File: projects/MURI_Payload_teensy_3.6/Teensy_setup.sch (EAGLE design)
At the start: 54 parts, among them IC1 DS18B20, IC2 DS18B20, IC4 DS18B20, IC5 DS18B20, U2 MS560702BA03-50

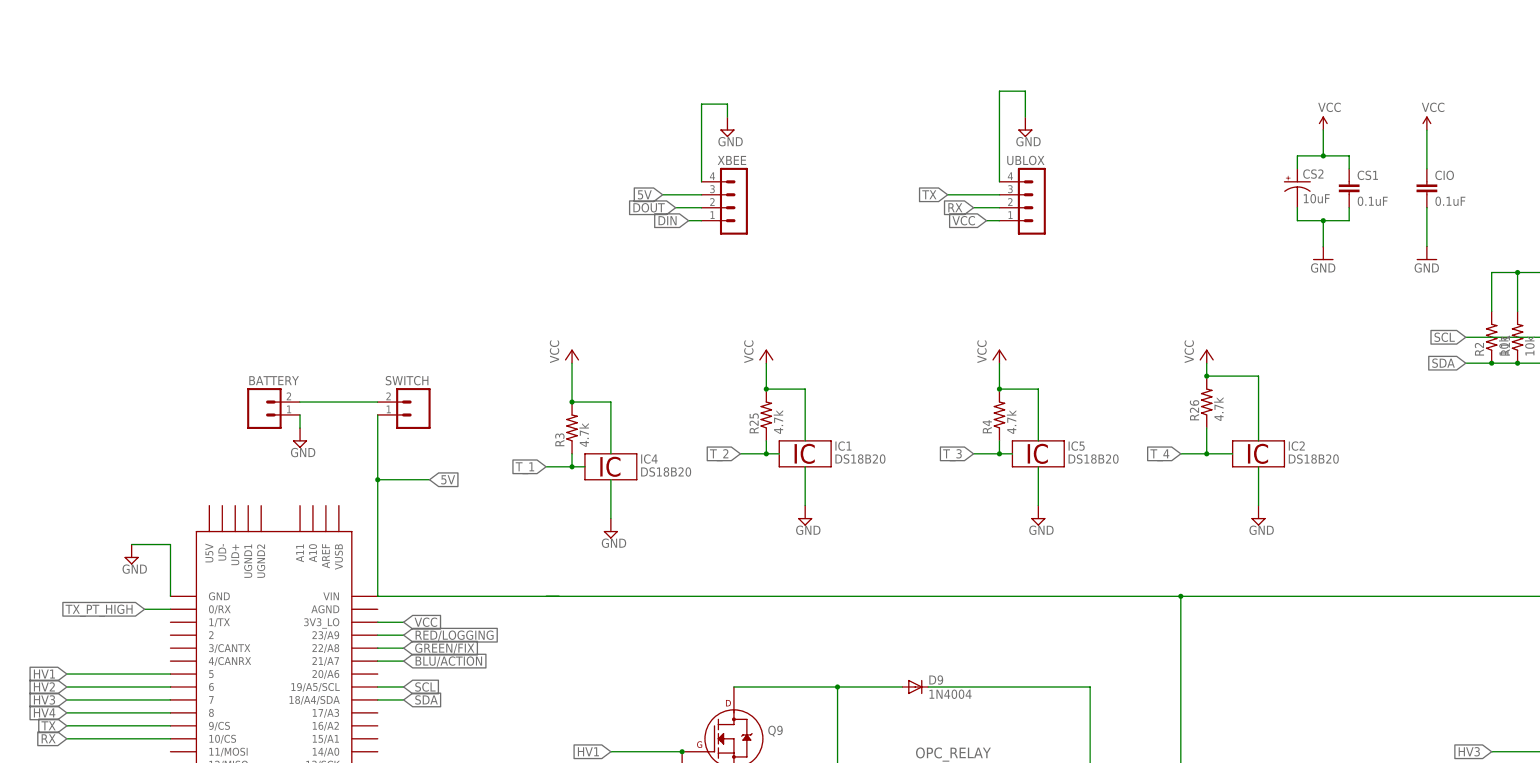
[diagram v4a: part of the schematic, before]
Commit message: I wired up the first iteration of the PCB and added terminal blocks to the schematic
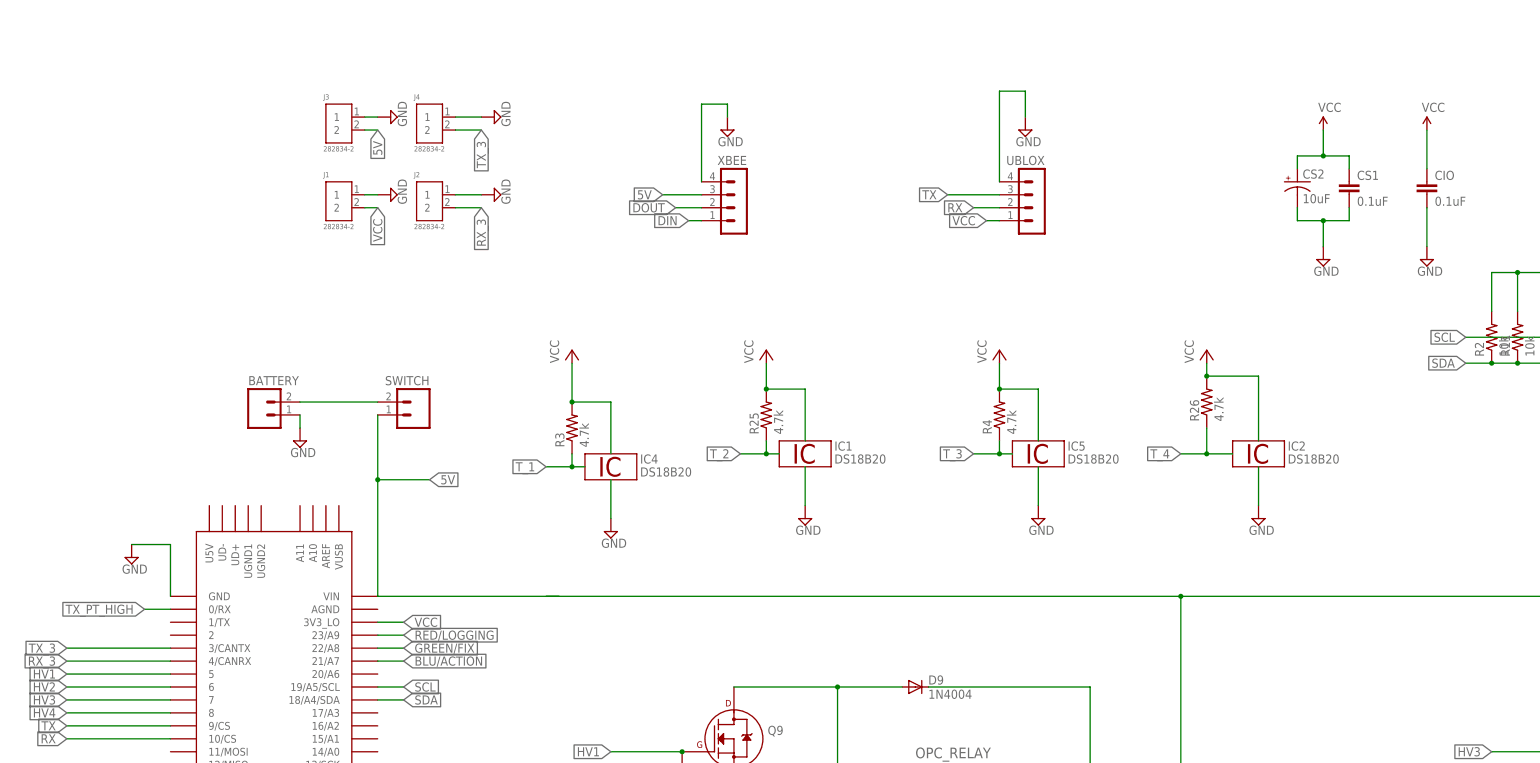
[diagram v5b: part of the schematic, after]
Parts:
- added J1, J2, J3, J4: 282834-2, 282834-2:282834-2
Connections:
- new net RX_3: J2.2, U$1.4/CANRX
- new net TX_3: J4.2, U$1.3/CANTX
- net 5V: now also J3.2
- net GND: now also J1.1, J2.1, J3.1, J4.1
- net VCC: now also J1.2
